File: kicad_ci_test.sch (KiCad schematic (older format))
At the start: 4 parts, among them J1 Conn_01x02_Female, J2 Conn_01x02_Female

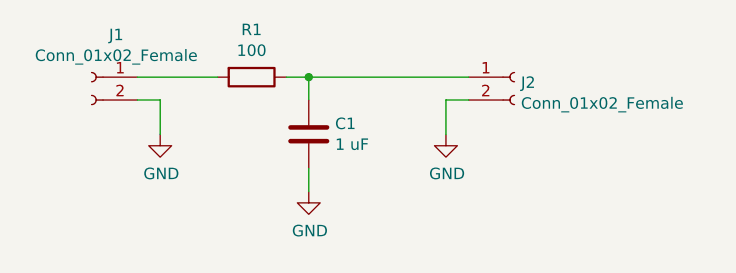
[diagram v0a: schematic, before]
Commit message: Added power flag to remove the ERC warning
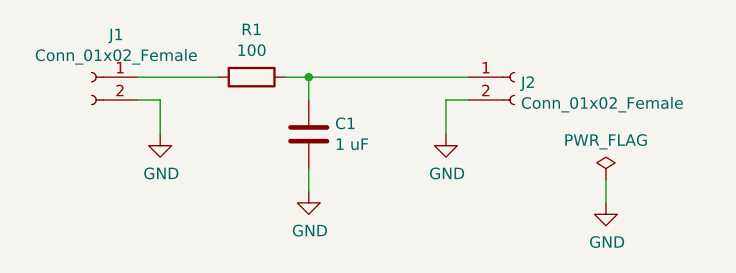
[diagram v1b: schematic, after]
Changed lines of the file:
@@
 	1    0    0    -1
 $EndComp
+$Comp
+L power:GND #PWR0101
+U 1 1 5E9E3B3B
+P 5550 3200
+F 0 "#PWR0101" H 5550 2950 50  0001 C CNN
+F 1 "GND" H 5555 3027 50  0000 C CNN
+F 2 "" H 5550 3200 50  0001 C CNN
+F 3 "" H 5550 3200 50  0001 C CNN
+	1    5550 3200
+	1    0    0    -1
+$EndComp
+$Comp
+L power:PWR_FLAG #FLG0101
+U 1 1 5E9E3D07
+P 5550 3100
+F 0 "#FLG0101" H 5550 3175 50  0001 C CNN
+F 1 "PWR_FLAG" H 5550 3273 50  0000 C CNN
+F 2 "" H 5550 3100 50  0001 C CNN
+F 3 "~" H 5550 3100 50  0001 C CNN
+	1    5550 3100
+	1    0    0    -1
+$EndComp
+Wire Wire Line
+	5550 3100 5550 3200
 $EndSCHEMATC
